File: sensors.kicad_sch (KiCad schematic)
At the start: 10 parts, among them J15 GND, J16 Sensor, J17 3.3v, J18 SDA, J19 SCL, U30 BMI270

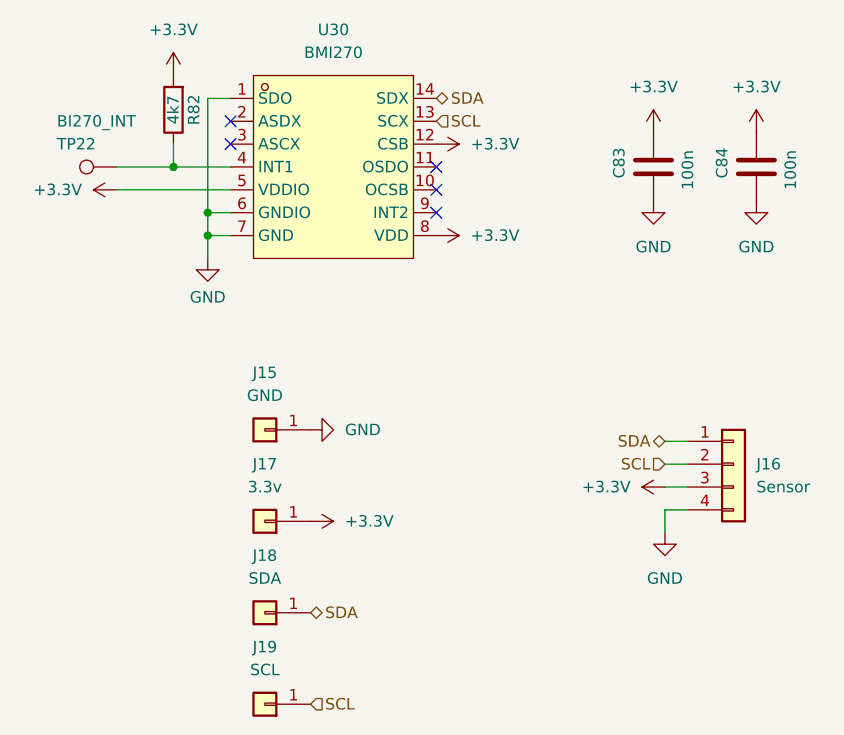
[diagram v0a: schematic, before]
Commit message: ESD protection on 3.3v for CATT connector, new LoRa module, compliance symbols
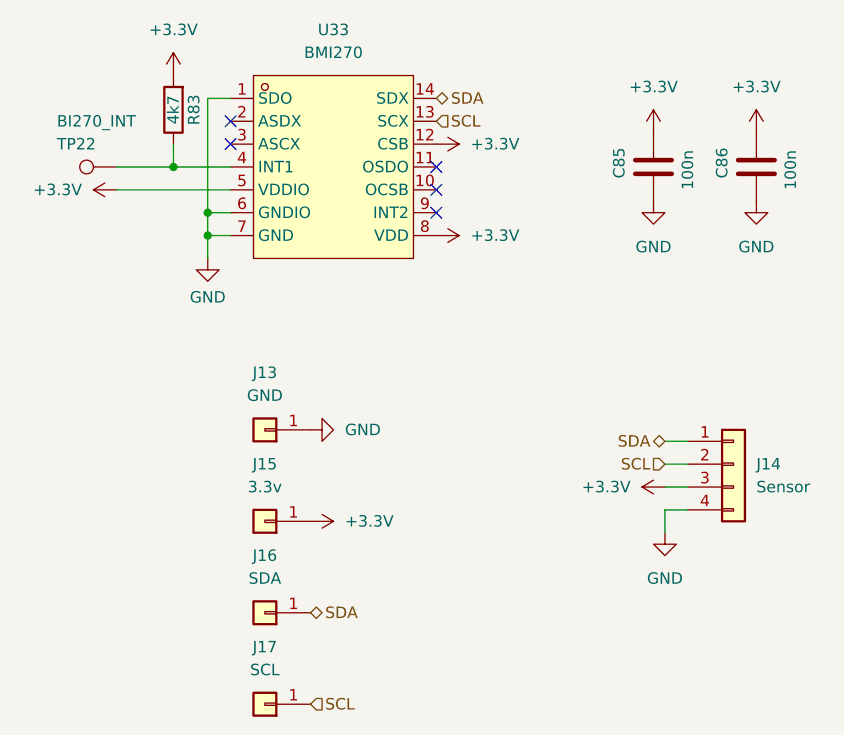
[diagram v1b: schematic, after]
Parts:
- renumbered C83 to C85, C84 to C86, J15 to J13, J16 to J14, J17 to J15, J18 to J16, J19 to J17, R82 to R83, U30 to U33
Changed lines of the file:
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@@
 (kicad_sch
-	(version 20231120)
+	(version 20250114)
 	(generator "eeschema")
-	(generator_version "8.0")
+	(generator_version "9.0")
 	(paper "A4")
 	(title_block
 		(title "Tanmatsu")
-		(date "2025-01-16")
+		(date "2025-02-26")
 		(rev "1.0")
 		(company "Nicolai Electronics")
@@
 		(shape bidirectional)
 		(at 88.9 64.77 180)
-		(fields_autoplaced yes)
 		(effects
 			(font
@@
 		(shape bidirectional)
 		(at 63.5 26.67 0)
-		(fields_autoplaced yes)
 		(effects
 			(font
@@
 		(shape input)
 		(at 49.53 93.98 0)
-		(fields_autoplaced yes)
 		(effects
 			(font
@@
 		(shape input)
 		(at 63.5 29.21 0)
-		(fields_autoplaced yes)
 		(effects
 			(font
@@
 		(shape bidirectional)
 		(at 49.53 83.82 0)
-		(fields_autoplaced yes)
 		(effects
 			(font
@@
 		(shape input)
 		(at 88.9 67.31 180)
-		(fields_autoplaced yes)
 		(effects
 			(font
@@
 		(dnp no)
 		(fields_autoplaced yes)
-		(property "Reference" "#PWR0293"
+		(property "Reference" "#PWR0298"
 			(at 45.72 73.66 0)
 			(effects
@@
 			(project "why2025"
 				(path "/6a31734e-65de-48f3-8156-2b24b665b183/14d9c0ee-00ab-4a1b-b059-e8045c71d6ae"
-					(reference "#PWR0293")
+					(reference "#PWR0298")
 					(unit 1)
 				)
@@
 		(on_board yes)
 		(dnp no)
-		(property "Reference" "#PWR0287"
+		(property "Reference" "#PWR0292"
 			(at 87.63 44.45 0)
 			(effects
@@
 			(project "why2025"
 				(path "/6a31734e-65de-48f3-8156-2b24b665b183/14d9c0ee-00ab-4a1b-b059-e8045c71d6ae"
-					(reference "#PWR0287")
+					(reference "#PWR0292")
 					(unit 1)
 				)
@@
 		(dnp no)
 		(fields_autoplaced yes)
-		(property "Reference" "J17"
+		(property "Reference" "J15"
 			(at 44.45 67.31 0)
 			(effects
@@
 			(project "why2025"
 				(path "/6a31734e-65de-48f3-8156-2b24b665b183/14d9c0ee-00ab-4a1b-b059-e8045c71d6ae"
-					(reference "J17")
+					(reference "J15")
 					(unit 1)
 				)
@@
 		(dnp no)
 		(fields_autoplaced yes)
-		(property "Reference" "#PWR0289"
+		(property "Reference" "#PWR0294"
 			(at 59.69 41.91 0)
 			(effects
@@
 			(project "why2025"
 				(path "/6a31734e-65de-48f3-8156-2b24b665b183/14d9c0ee-00ab-4a1b-b059-e8045c71d6ae"
-					(reference "#PWR0289")
+					(reference "#PWR0294")
 					(unit 1)
 				)
@@
 		(dnp no)
 		(fields_autoplaced yes)
-		(property "Reference" "#PWR0285"
+		(property "Reference" "#PWR0290"
 			(at 59.69 31.75 0)
 			(effects
@@
 			(project "why2025"
 				(path "/6a31734e-65de-48f3-8156-2b24b665b183/14d9c0ee-00ab-4a1b-b059-e8045c71d6ae"
-					(reference "#PWR0285")
+					(reference "#PWR0290")
 					(unit 1)
 				)
@@
 		(dnp no)
 		(fields_autoplaced yes)
-		(property "Reference" "J15"
+		(property "Reference" "J13"
 			(at 44.45 57.15 0)
 			(effects
@@
 			(project "why2025"
 				(path "/6a31734e-65de-48f3-8156-2b24b665b183/14d9c0ee-00ab-4a1b-b059-e8045c71d6ae"
-					(reference "J15")
+					(reference "J13")
 					(unit 1)
 				)
@@
 		(dnp no)
 		(fields_autoplaced yes)
-		(property "Reference" "#PWR0291"
+		(property "Reference" "#PWR0296"
 			(at 55.88 63.5 0)
 			(effects
@@
 			(project "why2025"
 				(path "/6a31734e-65de-48f3-8156-2b24b665b183/14d9c0ee-00ab-4a1b-b059-e8045c71d6ae"
-					(reference "#PWR0291")
+					(reference "#PWR0296")
 					(unit 1)
 				)
@@
 		(on_board yes)
 		(dnp no)
-		(property "Reference" "C83"
+		(property "Reference" "C85"
 			(at 83.82 35.56 90)
 			(effects
@@
 			(project "why2025"
 				(path "/6a31734e-65de-48f3-8156-2b24b665b183/14d9c0ee-00ab-4a1b-b059-e8045c71d6ae"
-					(reference "C83")
+					(reference "C85")
 					(unit 1)
 				)
@@
 		(dnp no)
 		(fields_autoplaced yes)
-		(property "Reference" "#PWR0283"
+		(property "Reference" "#PWR0288"
 			(at 87.63 34.29 0)
 			(effects
@@
 			(project "why2025"
 				(path "/6a31734e-65de-48f3-8156-2b24b665b183/14d9c0ee-00ab-4a1b-b059-e8045c71d6ae"
-					(reference "#PWR0283")
+					(reference "#PWR0288")
 					(unit 1)
 				)
@@
 		(dnp no)
 		(fields_autoplaced yes)
-		(property "Reference" "J16"
+		(property "Reference" "J14"
 			(at 99.06 67.3099 0)
 			(effects
@@
 			(project ""
 				(path "/6a31734e-65de-48f3-8156-2b24b665b183/14d9c0ee-00ab-4a1b-b059-e8045c71d6ae"
-					(reference "J16")
+					(reference "J14")
 					(unit 1)
 				)
@@
 		(dnp no)
 		(fields_autoplaced yes)
-		(property "Reference" "#PWR0284"
+		(property "Reference" "#PWR0289"
 			(at 99.06 34.29 0)
 			(effects
@@
 			(project "why2025"
 				(path "/6a31734e-65de-48f3-8156-2b24b665b183/14d9c0ee-00ab-4a1b-b059-e8045c71d6ae"
-					(reference "#PWR0284")
+					(reference "#PWR0289")
 					(unit 1)
 				)
@@
 		(dnp no)
 		(fields_autoplaced yes)
-		(property "Reference" "#PWR0292"
+		(property "Reference" "#PWR0297"
 			(at 92.71 69.85 0)
 			(effects
@@
 			(project "tanmatsu"
 				(path "/6a31734e-65de-48f3-8156-2b24b665b183/14d9c0ee-00ab-4a1b-b059-e8045c71d6ae"
-					(reference "#PWR0292")
+					(reference "#PWR0297")
 					(unit 1)
 				)
@@
 		(on_board yes)
 		(dnp no)
-		(property "Reference" "#PWR0290"
+		(property "Reference" "#PWR0295"
 			(at 38.1 50.8 0)
 			(effects
@@
 			(project "why2025"
 				(path "/6a31734e-65de-48f3-8156-2b24b665b183/14d9c0ee-00ab-4a1b-b059-e8045c71d6ae"
-					(reference "#PWR0290")
+					(reference "#PWR0295")
 					(unit 1)
 				)
@@
 		(dnp no)
 		(fields_autoplaced yes)
-		(property "Reference" "J19"
+		(property "Reference" "J17"
 			(at 44.45 87.63 0)
 			(effects
@@
 			(project "why2025"
 				(path "/6a31734e-65de-48f3-8156-2b24b665b183/14d9c0ee-00ab-4a1b-b059-e8045c71d6ae"
-					(reference "J19")
+					(reference "J17")
 					(unit 1)
 				)
@@
 		(dnp no)
 		(fields_autoplaced yes)
-		(property "Reference" "#PWR0286"
+		(property "Reference" "#PWR0291"
 			(at 31.75 36.83 0)
 			(effects
@@
 			(project "why2025"
 				(path "/6a31734e-65de-48f3-8156-2b24b665b183/14d9c0ee-00ab-4a1b-b059-e8045c71d6ae"
-					(reference "#PWR0286")
+					(reference "#PWR0291")
 					(unit 1)
 				)
@@
 		(dnp no)
 		(fields_autoplaced yes)
-		(property "Reference" "#PWR0294"
+		(property "Reference" "#PWR0299"
 			(at 88.9 81.28 0)
 			(effects
@@
 			(project "tanmatsu"
 				(path "/6a31734e-65de-48f3-8156-2b24b665b183/14d9c0ee-00ab-4a1b-b059-e8045c71d6ae"
-					(reference "#PWR0294")
+					(reference "#PWR0299")
 					(unit 1)
 				)
@@
 		(on_board yes)
 		(dnp no)
-		(property "Reference" "#PWR0288"
+		(property "Reference" "#PWR0293"
 			(at 99.06 44.45 0)
 			(effects
@@
 			(project "why2025"
 				(path "/6a31734e-65de-48f3-8156-2b24b665b183/14d9c0ee-00ab-4a1b-b059-e8045c71d6ae"
-					(reference "#PWR0288")
+					(reference "#PWR0293")
 					(unit 1)
 				)
@@
 		(on_board yes)
 		(dnp no)
-		(property "Reference" "R82"
+		(property "Reference" "R83"
 			(at 36.576 27.94 90)
 			(effects
@@
 			(project "why2025"
 				(path "/6a31734e-65de-48f3-8156-2b24b665b183/14d9c0ee-00ab-4a1b-b059-e8045c71d6ae"
-					(reference "R82")
+					(reference "R83")
 					(unit 1)
 				)
@@
 		(dnp no)
 		(fields_autoplaced yes)
-		(property "Reference" "J18"
+		(property "Reference" "J16"
 			(at 44.45 77.47 0)
 			(effects
@@
 			(project "why2025"
 				(path "/6a31734e-65de-48f3-8156-2b24b665b183/14d9c0ee-00ab-4a1b-b059-e8045c71d6ae"
-					(reference "J18")
+					(reference "J16")
 					(unit 1)
 				)
@@
 		(dnp no)
 		(fields_autoplaced yes)
-		(property "Reference" "#PWR0282"
+		(property "Reference" "#PWR0287"
 			(at 34.29 27.94 0)
 			(effects
@@
 			(project "why2025"
 				(path "/6a31734e-65de-48f3-8156-2b24b665b183/14d9c0ee-00ab-4a1b-b059-e8045c71d6ae"
-					(reference "#PWR0282")
+					(reference "#PWR0287")
 					(unit 1)
 				)
@@
 		(dnp no)
 		(fields_autoplaced yes)
-		(property "Reference" "U30"
+		(property "Reference" "U33"
 			(at 52.07 19.05 0)
 			(effects
@@
 			(project ""
 				(path "/6a31734e-65de-48f3-8156-2b24b665b183/14d9c0ee-00ab-4a1b-b059-e8045c71d6ae"
-					(reference "U30")
+					(reference "U33")
 					(unit 1)
 				)
@@
 		(on_board yes)
 		(dnp no)
-		(property "Reference" "C84"
+		(property "Reference" "C86"
 			(at 95.25 35.56 90)
 			(effects
@@
 			(project "why2025"
 				(path "/6a31734e-65de-48f3-8156-2b24b665b183/14d9c0ee-00ab-4a1b-b059-e8045c71d6ae"
-					(reference "C84")
-					(unit 1)
-				)
+					(reference "C86")
+					(unit 1)
+				)

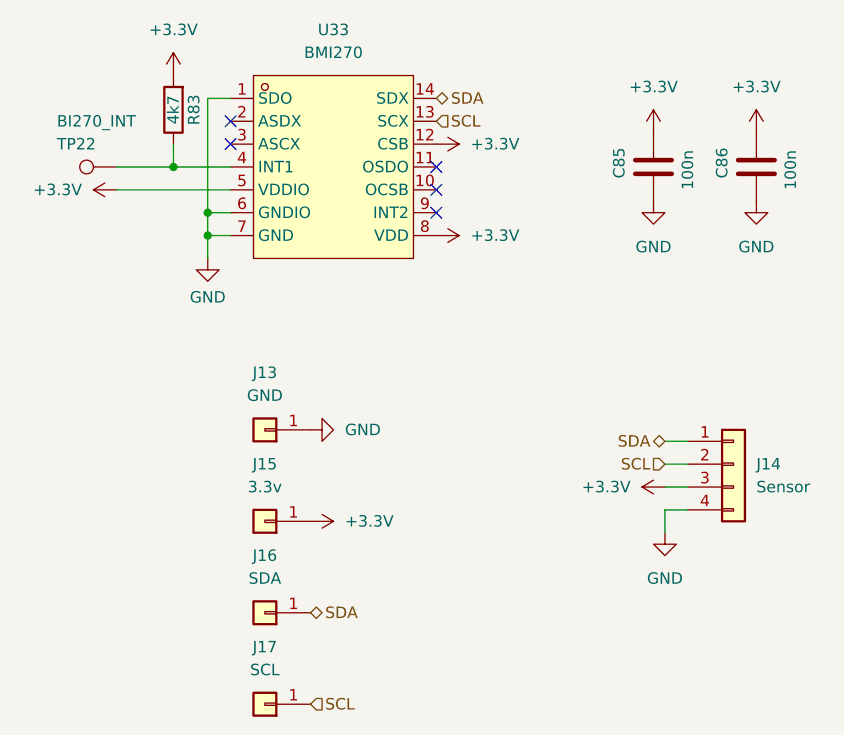
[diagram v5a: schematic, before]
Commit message: Reassign component designators and regenerate schematic + production files
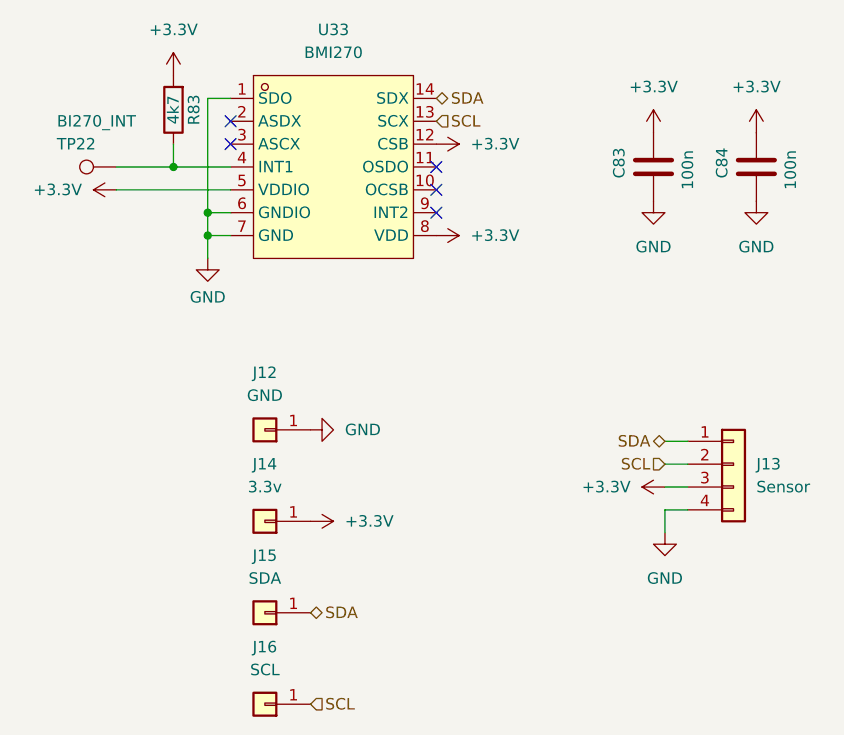
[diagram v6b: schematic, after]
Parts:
- renumbered C85 to C83, C86 to C84, J13 to J12, J14 to J13, J15 to J14, J16 to J15, J17 to J16
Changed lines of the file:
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@@
 		(dnp no)
 		(fields_autoplaced yes)
-		(property "Reference" "J15"
+		(property "Reference" "J14"
 			(at 44.45 67.31 0)
 			(effects
@@
 			(project "why2025"
 				(path "/6a31734e-65de-48f3-8156-2b24b665b183/14d9c0ee-00ab-4a1b-b059-e8045c71d6ae"
-					(reference "J15")
+					(reference "J14")
 					(unit 1)
 				)
@@
 		(dnp no)
 		(fields_autoplaced yes)
-		(property "Reference" "J13"
+		(property "Reference" "J12"
 			(at 44.45 57.15 0)
 			(effects
@@
 			(project "why2025"
 				(path "/6a31734e-65de-48f3-8156-2b24b665b183/14d9c0ee-00ab-4a1b-b059-e8045c71d6ae"
-					(reference "J13")
+					(reference "J12")
 					(unit 1)
 				)
@@
 		(on_board yes)
 		(dnp no)
-		(property "Reference" "C85"
+		(property "Reference" "C83"
 			(at 83.82 35.56 90)
 			(effects
@@
 			(project "why2025"
 				(path "/6a31734e-65de-48f3-8156-2b24b665b183/14d9c0ee-00ab-4a1b-b059-e8045c71d6ae"
-					(reference "C85")
+					(reference "C83")
 					(unit 1)
 				)
@@
 		(dnp no)
 		(fields_autoplaced yes)
-		(property "Reference" "J14"
+		(property "Reference" "J13"
 			(at 99.06 67.3099 0)
 			(effects
@@
 			(project ""
 				(path "/6a31734e-65de-48f3-8156-2b24b665b183/14d9c0ee-00ab-4a1b-b059-e8045c71d6ae"
-					(reference "J14")
+					(reference "J13")
 					(unit 1)
 				)
@@
 		(dnp no)
 		(fields_autoplaced yes)
-		(property "Reference" "J17"
+		(property "Reference" "J16"
 			(at 44.45 87.63 0)
 			(effects
@@
 			(project "why2025"
 				(path "/6a31734e-65de-48f3-8156-2b24b665b183/14d9c0ee-00ab-4a1b-b059-e8045c71d6ae"
-					(reference "J17")
+					(reference "J16")
 					(unit 1)
 				)
@@
 		(dnp no)
 		(fields_autoplaced yes)
-		(property "Reference" "J16"
+		(property "Reference" "J15"
 			(at 44.45 77.47 0)
 			(effects
@@
 			(project "why2025"
 				(path "/6a31734e-65de-48f3-8156-2b24b665b183/14d9c0ee-00ab-4a1b-b059-e8045c71d6ae"
-					(reference "J16")
+					(reference "J15")
 					(unit 1)
 				)
@@
 		(on_board yes)
 		(dnp no)
-		(property "Reference" "C86"
+		(property "Reference" "C84"
 			(at 95.25 35.56 90)
 			(effects
@@
 			(project "why2025"
 				(path "/6a31734e-65de-48f3-8156-2b24b665b183/14d9c0ee-00ab-4a1b-b059-e8045c71d6ae"
-					(reference "C86")
-					(unit 1)
-				)
+					(reference "C84")
+					(unit 1)
+				)

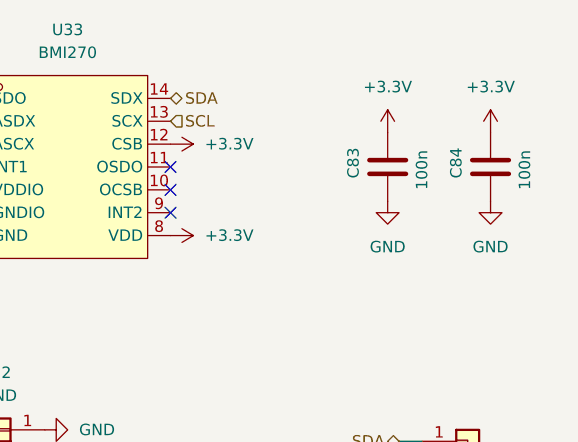
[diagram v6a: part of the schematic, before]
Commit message: Move LoRa module, add capacitor, finalize design for production
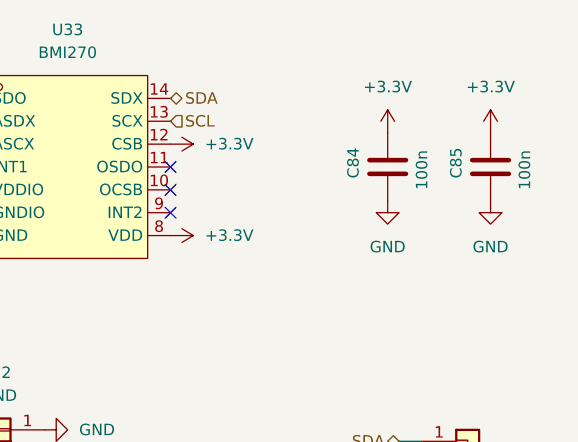
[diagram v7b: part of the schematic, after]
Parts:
- renumbered C83 to C84, C84 to C85
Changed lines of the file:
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@@
 	(title_block
 		(title "Tanmatsu")
-		(date "2025-03-18")
+		(date "2025-04-04")
 		(rev "1.0")
 		(company "Nicolai Electronics")
@@
 		(dnp no)
 		(fields_autoplaced yes)
-		(property "Reference" "#PWR0298"
+		(property "Reference" "#PWR0299"
 			(at 45.72 73.66 0)
 			(effects
@@
 			(project "why2025"
 				(path "/6a31734e-65de-48f3-8156-2b24b665b183/14d9c0ee-00ab-4a1b-b059-e8045c71d6ae"
-					(reference "#PWR0298")
+					(reference "#PWR0299")
 					(unit 1)
 				)
@@
 		(on_board yes)
 		(dnp no)
-		(property "Reference" "#PWR0292"
+		(property "Reference" "#PWR0293"
 			(at 87.63 44.45 0)
 			(effects
@@
 			(project "why2025"
 				(path "/6a31734e-65de-48f3-8156-2b24b665b183/14d9c0ee-00ab-4a1b-b059-e8045c71d6ae"
-					(reference "#PWR0292")
+					(reference "#PWR0293")
 					(unit 1)
 				)
@@
 		(dnp no)
 		(fields_autoplaced yes)
-		(property "Reference" "#PWR0294"
+		(property "Reference" "#PWR0295"
 			(at 59.69 41.91 0)
 			(effects
@@
 			(project "why2025"
 				(path "/6a31734e-65de-48f3-8156-2b24b665b183/14d9c0ee-00ab-4a1b-b059-e8045c71d6ae"
-					(reference "#PWR0294")
+					(reference "#PWR0295")
 					(unit 1)
 				)
@@
 		(dnp no)
 		(fields_autoplaced yes)
-		(property "Reference" "#PWR0290"
+		(property "Reference" "#PWR0291"
 			(at 59.69 31.75 0)
 			(effects
@@
 			(project "why2025"
 				(path "/6a31734e-65de-48f3-8156-2b24b665b183/14d9c0ee-00ab-4a1b-b059-e8045c71d6ae"
-					(reference "#PWR0290")
+					(reference "#PWR0291")
 					(unit 1)
 				)
@@
 		(dnp no)
 		(fields_autoplaced yes)
-		(property "Reference" "#PWR0296"
+		(property "Reference" "#PWR0297"
 			(at 55.88 63.5 0)
 			(effects
@@
 			(project "why2025"
 				(path "/6a31734e-65de-48f3-8156-2b24b665b183/14d9c0ee-00ab-4a1b-b059-e8045c71d6ae"
-					(reference "#PWR0296")
+					(reference "#PWR0297")
 					(unit 1)
 				)
@@
 		(on_board yes)
 		(dnp no)
-		(property "Reference" "C83"
+		(property "Reference" "C84"
 			(at 83.82 35.56 90)
 			(effects
@@
 			(project "why2025"
 				(path "/6a31734e-65de-48f3-8156-2b24b665b183/14d9c0ee-00ab-4a1b-b059-e8045c71d6ae"
-					(reference "C83")
+					(reference "C84")
 					(unit 1)
 				)
@@
 		(dnp no)
 		(fields_autoplaced yes)
-		(property "Reference" "#PWR0288"
+		(property "Reference" "#PWR0289"
 			(at 87.63 34.29 0)
 			(effects
@@
 			(project "why2025"
 				(path "/6a31734e-65de-48f3-8156-2b24b665b183/14d9c0ee-00ab-4a1b-b059-e8045c71d6ae"
-					(reference "#PWR0288")
+					(reference "#PWR0289")
 					(unit 1)
 				)
@@
 		(dnp no)
 		(fields_autoplaced yes)
-		(property "Reference" "#PWR0289"
+		(property "Reference" "#PWR0290"
 			(at 99.06 34.29 0)
 			(effects
@@
 			(project "why2025"
 				(path "/6a31734e-65de-48f3-8156-2b24b665b183/14d9c0ee-00ab-4a1b-b059-e8045c71d6ae"
-					(reference "#PWR0289")
+					(reference "#PWR0290")
 					(unit 1)
 				)
@@
 		(dnp no)
 		(fields_autoplaced yes)
-		(property "Reference" "#PWR0297"
+		(property "Reference" "#PWR0298"
 			(at 92.71 69.85 0)
 			(effects
@@
 			(project "tanmatsu"
 				(path "/6a31734e-65de-48f3-8156-2b24b665b183/14d9c0ee-00ab-4a1b-b059-e8045c71d6ae"
-					(reference "#PWR0297")
+					(reference "#PWR0298")
 					(unit 1)
 				)
@@
 		(on_board yes)
 		(dnp no)
-		(property "Reference" "#PWR0295"
+		(property "Reference" "#PWR0296"
 			(at 38.1 50.8 0)
 			(effects
@@
 			(project "why2025"
 				(path "/6a31734e-65de-48f3-8156-2b24b665b183/14d9c0ee-00ab-4a1b-b059-e8045c71d6ae"
-					(reference "#PWR0295")
+					(reference "#PWR0296")
 					(unit 1)
 				)
@@
 		(dnp no)
 		(fields_autoplaced yes)
-		(property "Reference" "#PWR0291"
+		(property "Reference" "#PWR0292"
 			(at 31.75 36.83 0)
 			(effects
@@
 			(project "why2025"
 				(path "/6a31734e-65de-48f3-8156-2b24b665b183/14d9c0ee-00ab-4a1b-b059-e8045c71d6ae"
-					(reference "#PWR0291")
+					(reference "#PWR0292")
 					(unit 1)
 				)
@@
 		(dnp no)
 		(fields_autoplaced yes)
-		(property "Reference" "#PWR0299"
+		(property "Reference" "#PWR0300"
 			(at 88.9 81.28 0)
 			(effects
@@
 			(project "tanmatsu"
 				(path "/6a31734e-65de-48f3-8156-2b24b665b183/14d9c0ee-00ab-4a1b-b059-e8045c71d6ae"
-					(reference "#PWR0299")
+					(reference "#PWR0300")
 					(unit 1)
 				)
@@
 		(on_board yes)
 		(dnp no)
-		(property "Reference" "#PWR0293"
+		(property "Reference" "#PWR0294"
 			(at 99.06 44.45 0)
 			(effects
@@
 			(project "why2025"
 				(path "/6a31734e-65de-48f3-8156-2b24b665b183/14d9c0ee-00ab-4a1b-b059-e8045c71d6ae"
-					(reference "#PWR0293")
+					(reference "#PWR0294")
 					(unit 1)
 				)
@@
 		(dnp no)
 		(fields_autoplaced yes)
-		(property "Reference" "#PWR0287"
+		(property "Reference" "#PWR0288"
 			(at 34.29 27.94 0)
 			(effects
@@
 			(project "why2025"
 				(path "/6a31734e-65de-48f3-8156-2b24b665b183/14d9c0ee-00ab-4a1b-b059-e8045c71d6ae"
-					(reference "#PWR0287")
+					(reference "#PWR0288")
 					(unit 1)
 				)
@@
 		(on_board yes)
 		(dnp no)
-		(property "Reference" "C84"
+		(property "Reference" "C85"
 			(at 95.25 35.56 90)
 			(effects
@@
 			(project "why2025"
 				(path "/6a31734e-65de-48f3-8156-2b24b665b183/14d9c0ee-00ab-4a1b-b059-e8045c71d6ae"
-					(reference "C84")
-					(unit 1)
-				)
+					(reference "C85")
+					(unit 1)
+				)
